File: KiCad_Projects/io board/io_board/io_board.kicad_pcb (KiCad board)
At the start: 2 copper layers, 78.4 x 100.1 mm, 15 parts, among them J1 Conn_01x13_Female, SW1 SW_Push, SW2 SW_Push, SW3 SW_Push, SW4 SW_Push, SW5 SW_DIP_x01, U1 LCD_Module

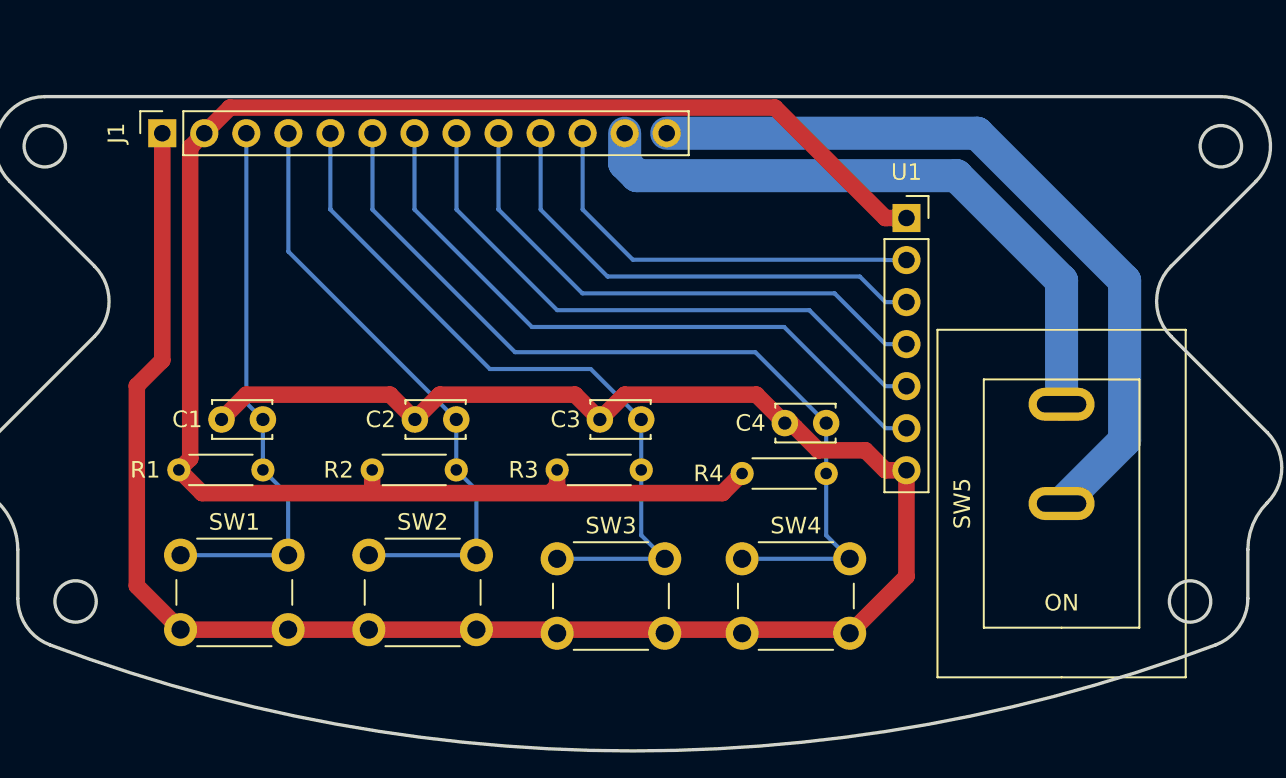
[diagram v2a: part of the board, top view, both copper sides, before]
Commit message: 部内大会用プログラムの作成
部内大会というか、北九州オープンくらいまでのプログラムが入ってます。
カメラ・IR_ring・Line_ringの制御。
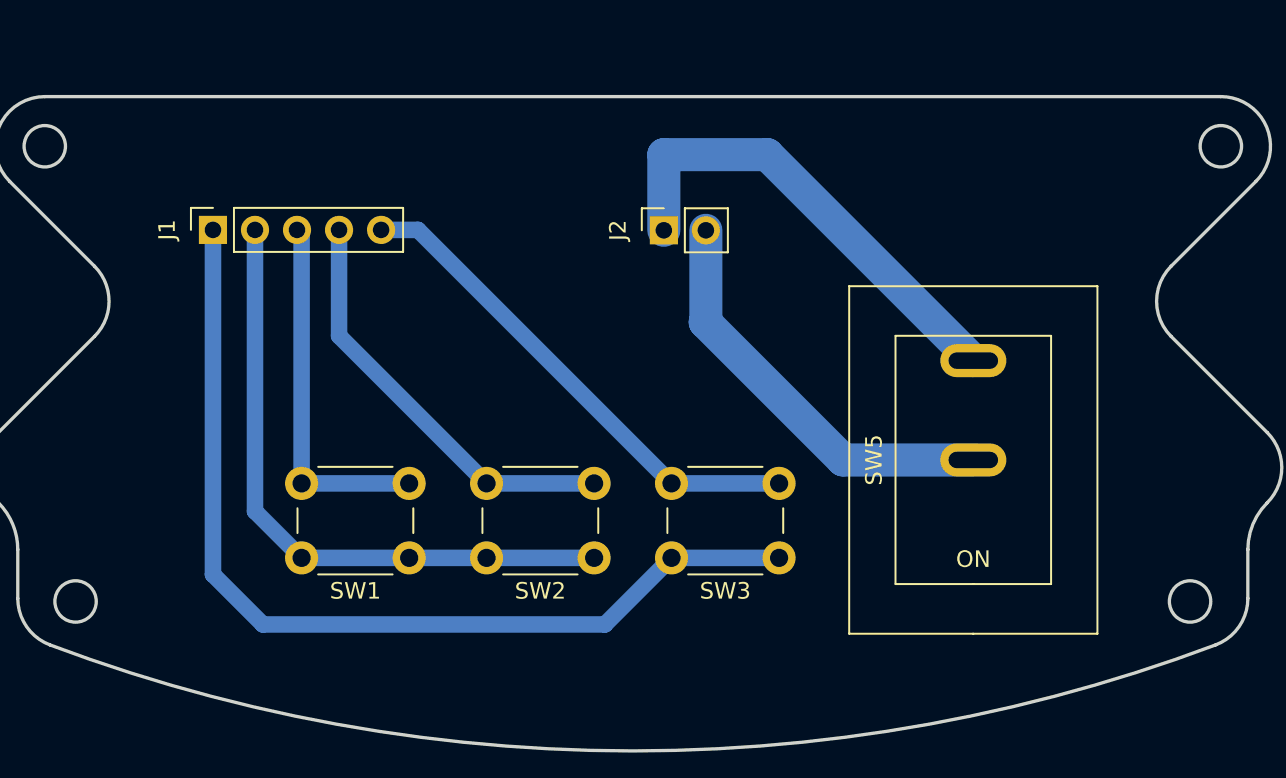
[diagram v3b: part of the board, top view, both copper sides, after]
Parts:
- removed C1, C2, C3, C4: C_Small, Capacitor_THT:C_Disc_D3.4mm_W2.1mm_P2.50mm
- removed R1, R2, R3, R4: R, Resistor_THT:R_Axial_DIN0204_L3.6mm_D1.6mm_P5.08mm_Horizontal
- removed SW4: SW_Push, Button_Switch_THT:SW_PUSH_6mm
- removed U1: LCD_Module, Connector_PinSocket_2.54mm:PinSocket_1x07_P2.54mm_Vertical
- added J2: Conn_01x02_Female, Connector_PinSocket_2.54mm:PinSocket_1x02_P2.54mm_Vertical, F.Cu at (156.3, 56.1)
- J1: value Conn_01x13_Female -> Conn_01x05_Female; footprint Connector_PinSocket_2.54mm:PinSocket_1x13_P2.54mm_Vertical -> Connector_PinSocket_2.54mm:PinSocket_1x05_P2.54mm_Vertical
- moved SW1 13.8 mm to (140.9, 75.9), turned to 180 degrees
- moved SW2 13.6 mm to (152.1, 75.9), turned to 180 degrees
- moved SW3 13.4 mm to (163.3, 75.9), turned to 180 degrees
- moved J1 6.60 mm to (129.1, 56.1)
- moved SW5 5.95 mm to (175.0, 70.0)
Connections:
- J1 pad 1: GND -> +5V
- J1 pad 2: +5V -> GND
- SW1 pad 1: SW1 -> GND
- SW1 pad 2: GND -> SW1
- SW2 pad 1: SW2 -> GND
- SW2 pad 2: GND -> SW2
- SW3 pad 1: SW3 -> +5V
- SW3 pad 2: GND -> SW3
- SW5 pad 2: GND1 -> GND
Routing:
- net GND: track 171.4 -> 67.1 mm
- net +5V: track 141.0 -> 57.9 mm
- net SW4: track 52.7 -> 0.00 mm
- net SDI: track 39.8 -> 0.00 mm
- net GND1: track 38.6 -> 0.00 mm
- net SCLK: track 36.2 -> 0.00 mm
- net RS: track 32.6 -> 0.00 mm
- net RE: track 29.0 -> 0.00 mm
- net CS: track 25.4 -> 0.00 mm
- net +7.5V: track 46.4 -> 25.2 mm
- net SW3: track 44.2 -> 30.4 mm
- net SW2: track 36.7 -> 25.5 mm
- net SW1: track 33.0 -> 22.3 mm
